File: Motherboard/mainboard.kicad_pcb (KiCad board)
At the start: 4 copper layers, 45.2 x 36 mm, 51 parts, among them IC1 BMX160, J1 Conn_01x01, J2 10118194-0001LF, J28 Conn_01x01, J29 Conn_01x01, J3 Micro_SD_Card, J30 Conn_01x01, J4 xf2m-2415-1a, J5 XF2M-1015-1A, J6 U.FL-R-SMT-1, J7 U.FL-R-SMT-1, J8 Conn_01x01, SW1 KMR231NG LFS, U1 RFM95W-915S2, U2 ATSAMD51G_TQFN48, U3 DRV8848, U4 TPS82740BSIPR, U5 DRV8848, U6 MAX708RESA-T, U8 RFM95W-915S2

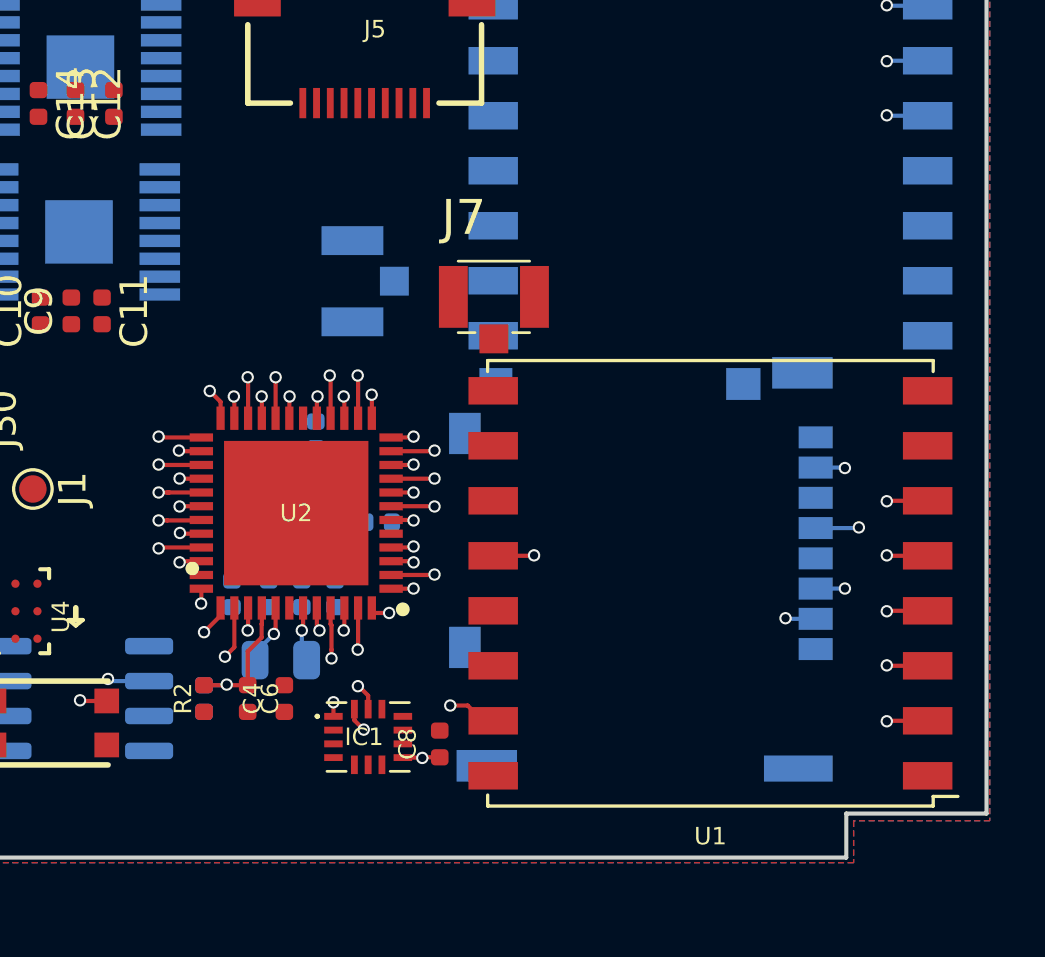
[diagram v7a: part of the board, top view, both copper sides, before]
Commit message: routing ~80%
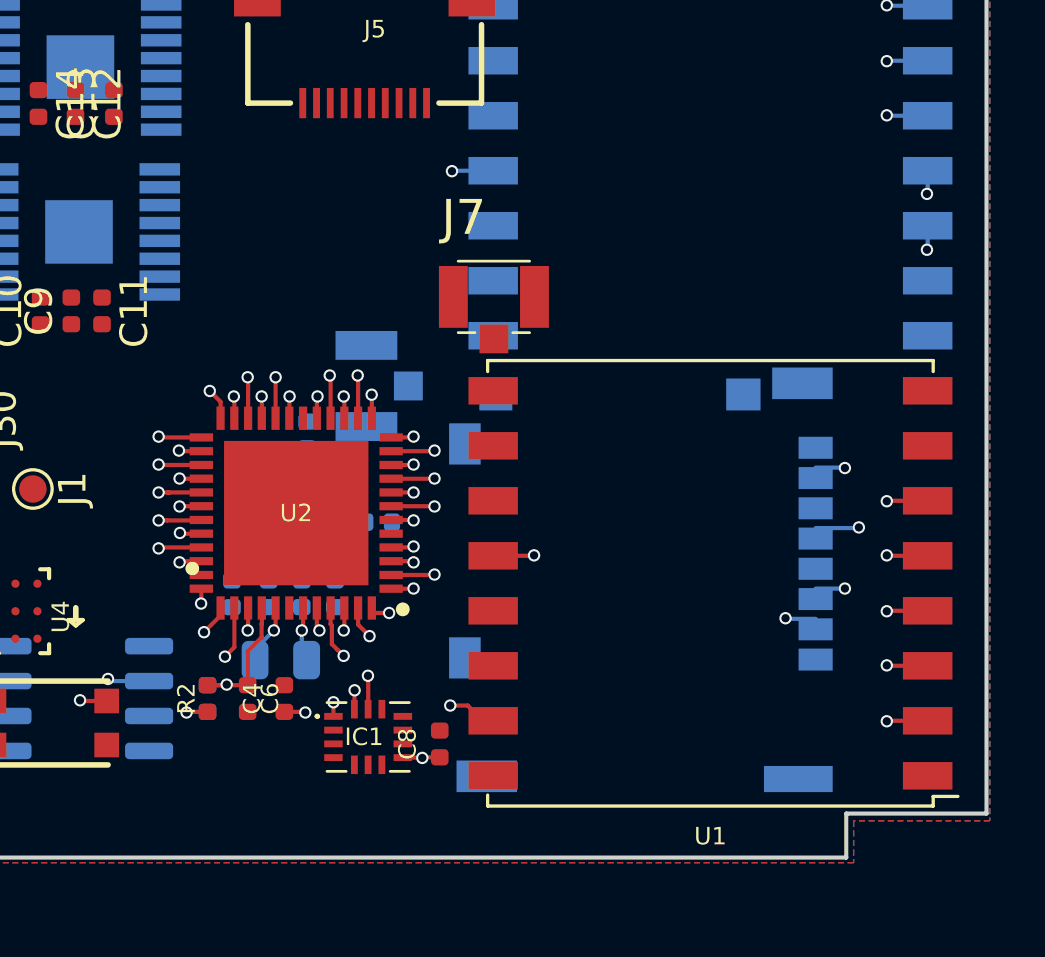
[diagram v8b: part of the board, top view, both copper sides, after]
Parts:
- moved J6 3.84 mm to (99.3, 92.4)
- moved J3 0.38 mm to (110.0, 99.4)
- moved C3 0.32 mm to (97.1, 94.2)
- moved R2 0.13 mm to (93.5, 103.8)
- moved R3 0.13 mm to (93.5, 103.8)
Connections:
- U2 pad 37: WDT_WDI -> Net-(U2-Pad37)
- U2 pad 38: Net-(U2-Pad38) -> WDT_WDI
- U2 pad 39: Net-(U2-Pad39) -> RF2_BUSY
- U2 pad 47: Net-(U2-Pad47) -> CS_SD
- U2 pad 48: Net-(U2-Pad48) -> RF2_CS
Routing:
- net Net-(U2-Pad47): track 17.0 -> 0.00 mm, vias 1 -> 0
- net CS_SD: track 1.11 -> 17.7 mm, vias 1 -> 2
- net Net-(U2-Pad19): track 0.80 -> 16.4 mm
- net Net-(U2-Pad20): track 1.49 -> 15.5 mm
- net Net-(U2-Pad37): track 0.00 -> 14.0 mm, vias 0 -> 1
- net Net-(U2-Pad24): track 5.58 -> 17.8 mm
- net Net-(U2-Pad11): track 1.59 -> 12.6 mm
- net Net-(U2-Pad12): track 0.83 -> 11.4 mm
- net Net-(U2-Pad30): track 8.88 -> 16.8 mm
- net RF2_BUSY: track 6.80 -> 14.0 mm, vias 1 -> 2
- net Net-(U2-Pad39): track 6.31 -> 0.00 mm, vias 1 -> 0
- net Net-(U2-Pad32): track 16.6 -> 10.4 mm
- net Net-(U2-Pad27): track 15.6 -> 9.75 mm
- net Net-(U2-Pad38): track 5.81 -> 0.00 mm, vias 1 -> 0
- net Net-(U2-Pad23): track 11.5 -> 5.75 mm
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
